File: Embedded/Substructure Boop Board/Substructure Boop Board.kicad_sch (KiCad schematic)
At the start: 22 parts, among them U1 PN5321A3HN_C1xx, U2 AD7142ACPZ-500RL7, U3 LD1117S33TR_SOT223, U5 R FFC, Y1 7M-27.120MAAJ-T

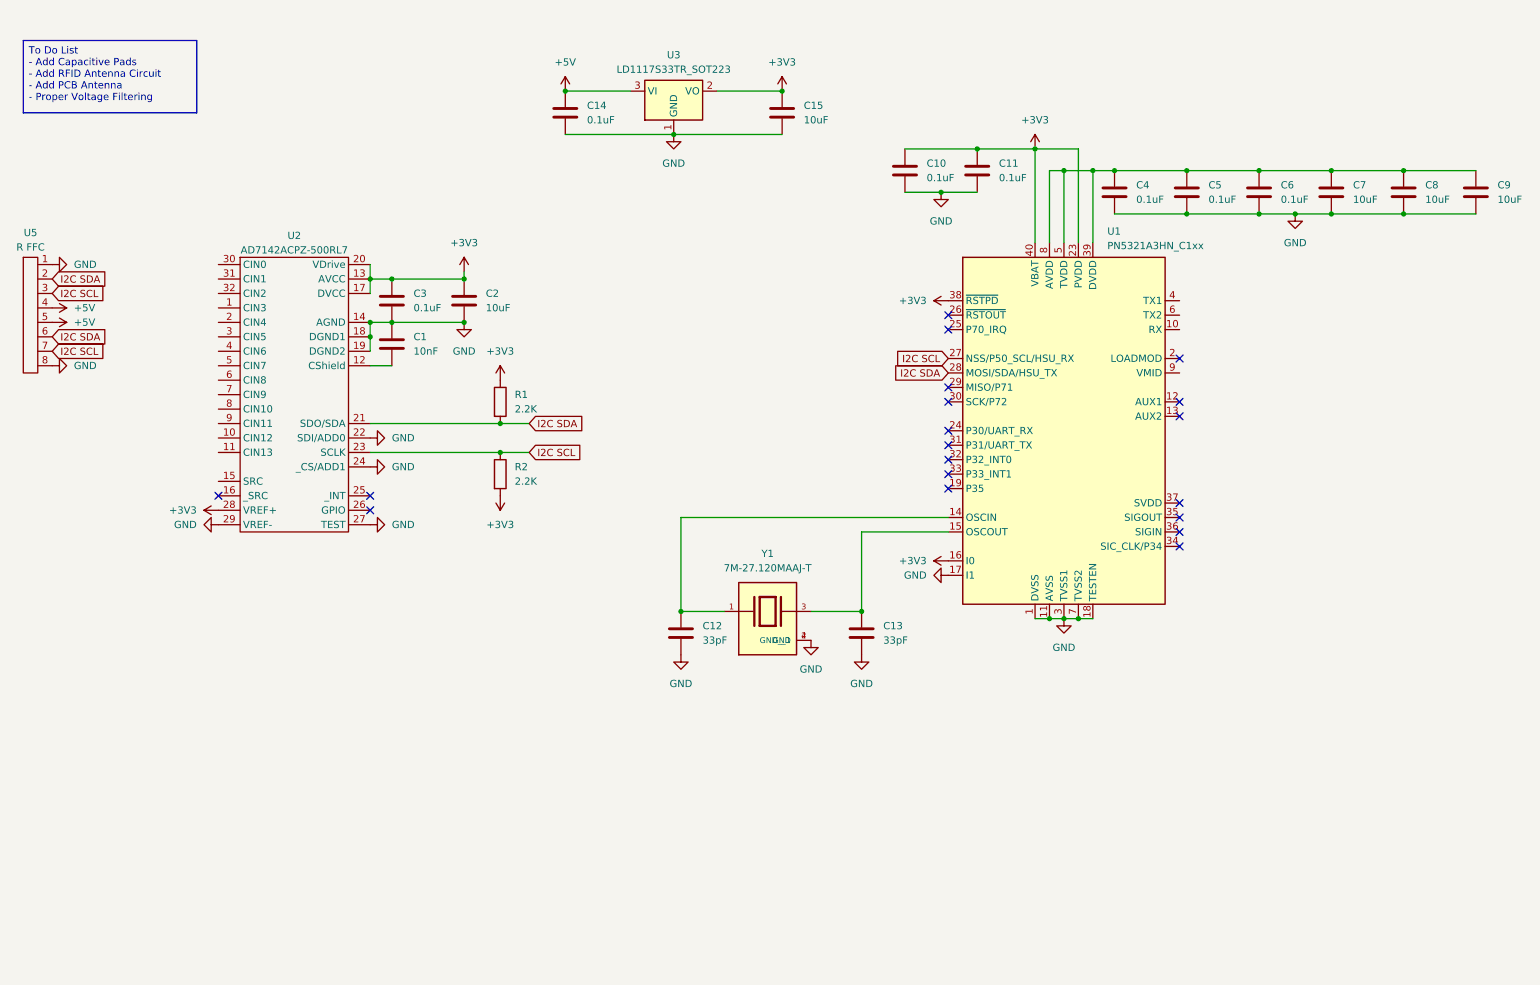
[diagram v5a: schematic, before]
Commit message: Added Antenna matching circuit
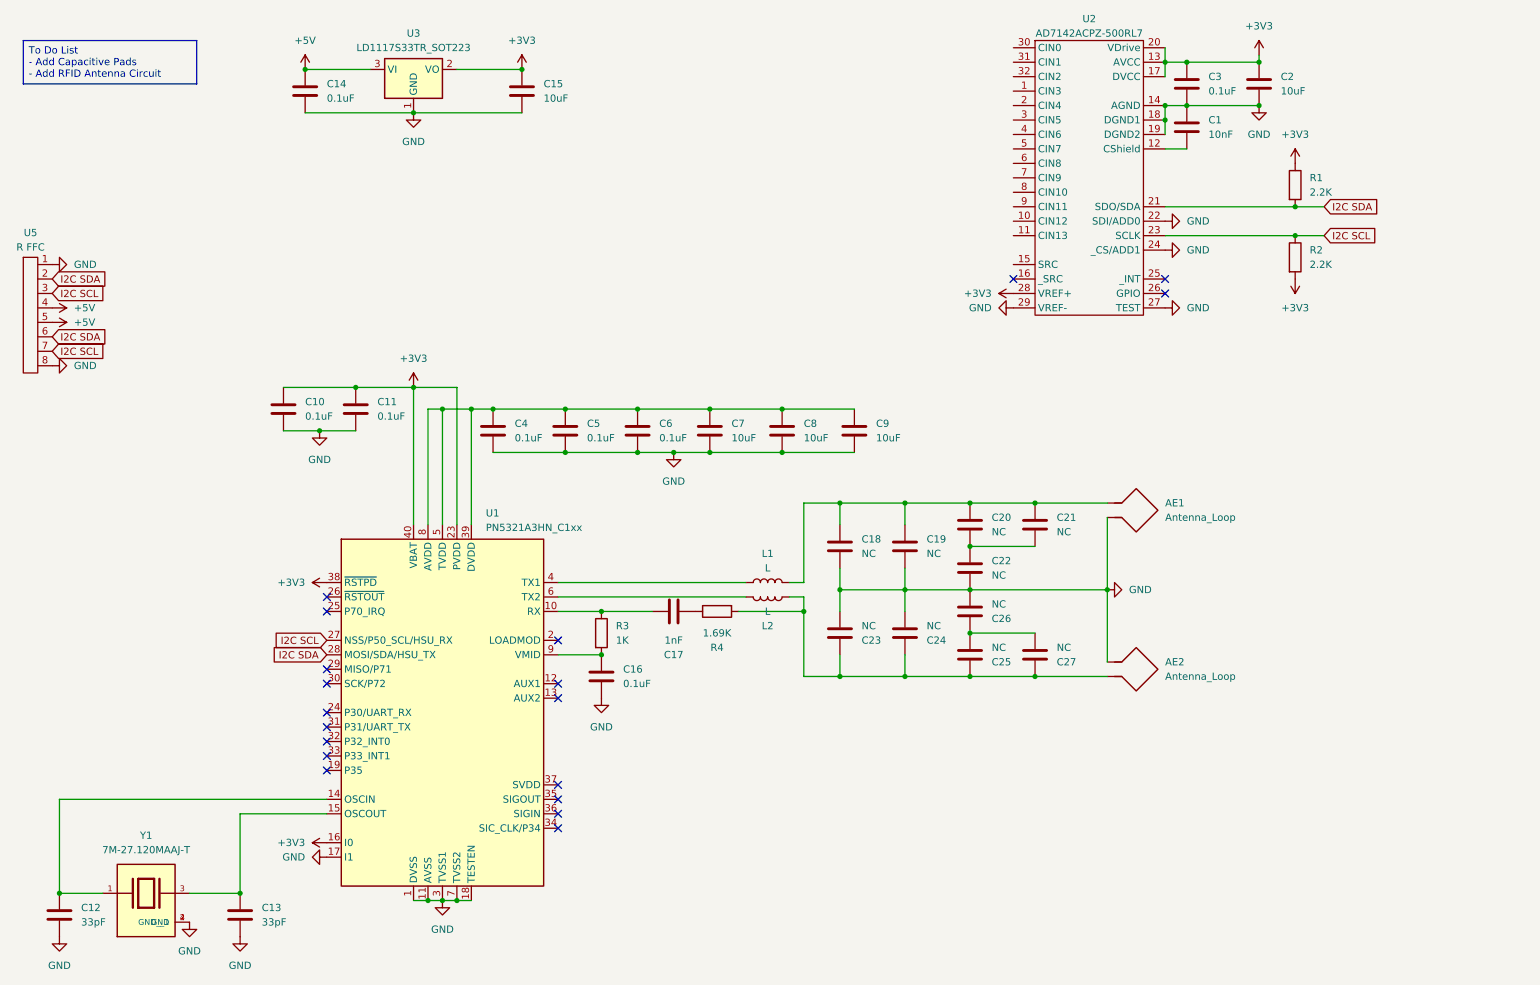
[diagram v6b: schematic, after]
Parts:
- added AE1, AE2: Antenna_Loop, symbol Device:Antenna_Loop
- added C16: 0.1uF, Capacitor_SMD:C_0603_1608Metric_Pad1.08x0.95mm_HandSolder, symbol Device:C
- added C17: 1nF, Capacitor_SMD:C_0603_1608Metric_Pad1.08x0.95mm_HandSolder, symbol Device:C
- added C18, C19, C20, C21, C22, C23, C24, C25, C26, C27: NC, Capacitor_SMD:C_0603_1608Metric_Pad1.08x0.95mm_HandSolder, symbol Device:C
- added L1, L2: L, symbol Device:L
- added R3: 1K, Resistor_SMD:R_0603_1608Metric_Pad0.98x0.95mm_HandSolder, symbol Device:R
- added R4: 1.69K, Resistor_SMD:R_0603_1608Metric_Pad0.98x0.95mm_HandSolder, symbol Device:R
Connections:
- net GND: now also AE1.2, AE2.1, C16.2, C18.2, C19.2, C22.2, C23.2, C24.2, C26.2
- net at U1.10 (RX): now also C17.1, R3.1
- net at U1.4 (TX1): now also L1.1
- net at U1.6 (TX2): now also L2.1
- net at U1.9 (VMID): now also C16.1, R3.2
- new net: AE1.1, C18.1, C19.1, C20.1, C21.1, L1.2
- new net: C20.2, C21.2, C22.1
- new net: AE2.2, C23.1, C24.1, C25.1, C27.1, L2.2, R4.2
- new net: C17.2, R4.1
- new net: C25.2, C26.1, C27.2
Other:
- moved on the sheet: C1, C10, C11, C12, C13, C14, C15, C2, C3, C4, C5, C6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

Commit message: Added Capacitive touch pads to schematic
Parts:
- added TP1, TP2: Touch Pad, symbol Connector:TestPoint_2Pole
- Y1: DIGIKEY (none) -> 887-1424-1-ND
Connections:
- net GND: now also TP1.1, TP2.1

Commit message: Added Component placement ideation
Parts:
- U5: footprint FFC:FFC-8-0.5 -> FFC:FFC 0.8mm 8P
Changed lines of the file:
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@@
 			)
 		)
-		(property "Footprint" "FFC:FFC-8-0.5"
+		(property "Footprint" "FFC:FFC 0.8mm 8P"
 			(at 26.67 72.39 0)
 			(effects
